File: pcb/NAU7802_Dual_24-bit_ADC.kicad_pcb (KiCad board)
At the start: 2 copper layers, 50.8 x 22.9 mm, 36 parts, among them J1 CELL_A, J2 CELL_B, J3 STEMMA_QT, J4 STEMMA_QT, M1 Feather_M4_Express, U1 NAU7802

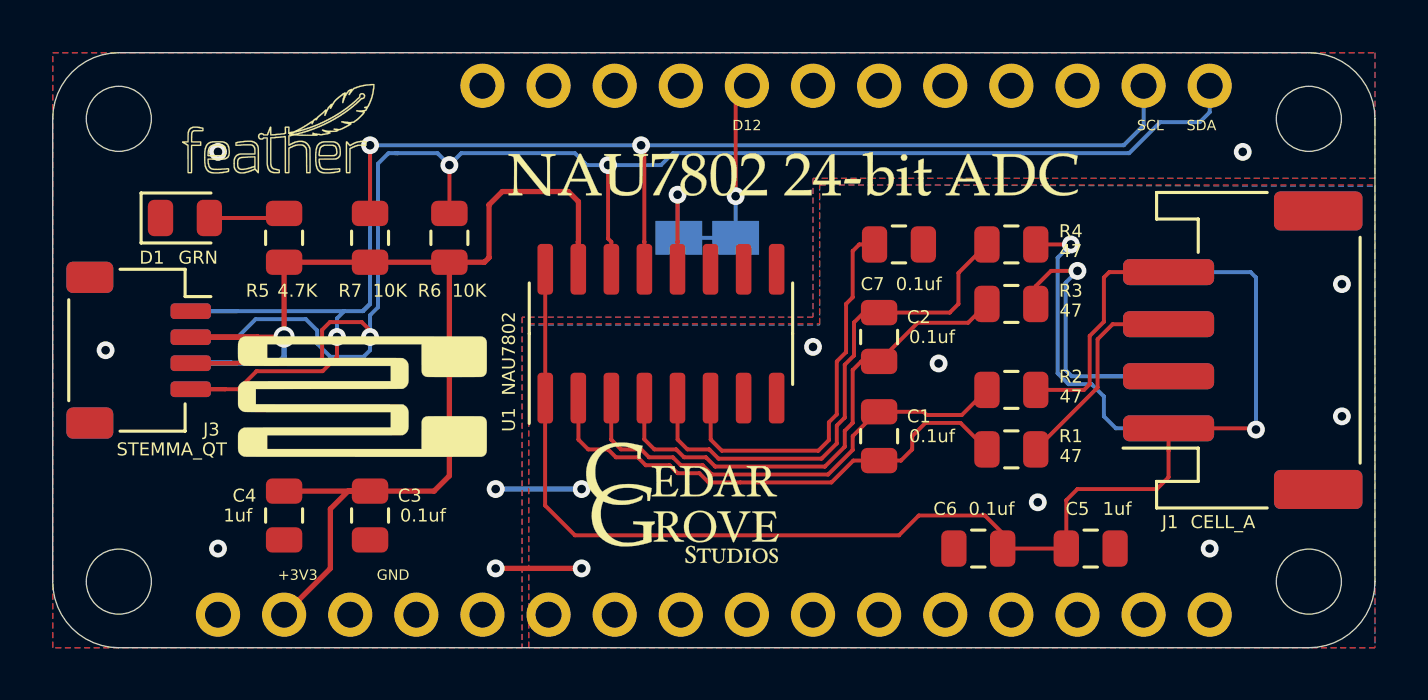
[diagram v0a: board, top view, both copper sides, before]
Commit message: update for 2-channel operation
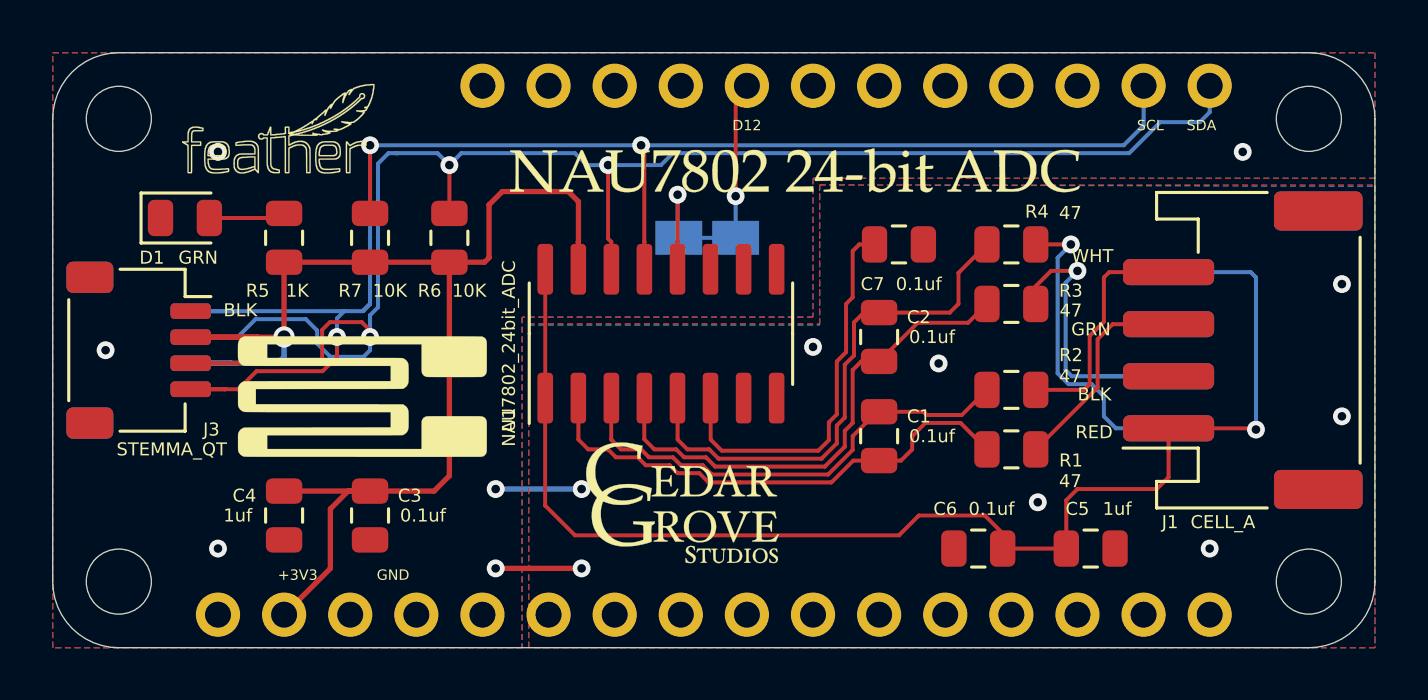
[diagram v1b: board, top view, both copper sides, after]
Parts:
- R5: value 4.7K -> 1K
- U1: value NAU7802 -> NAU7802_24bit_ADC
- moved G*** 0.15 mm to (156.8, 94.7)
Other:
- board text added: "2020-11-26 v01"
- board text added: "BLK"
- board text added: "GRN"
- board text added: "RED"
- board text added: "WHT"
- board text removed: "2020-10-21 v00"

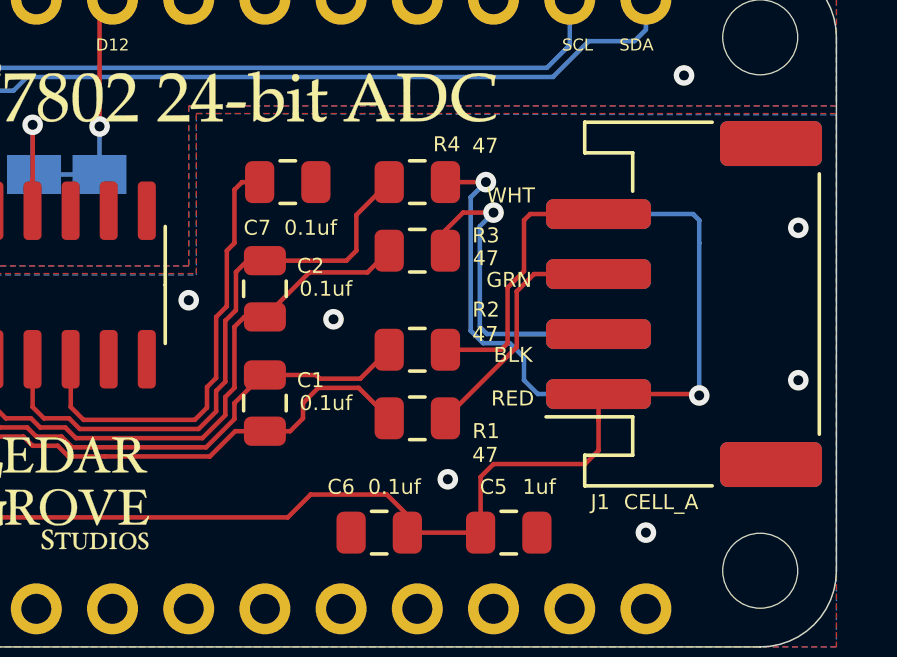
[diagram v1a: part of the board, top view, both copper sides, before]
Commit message: update PCB silk design
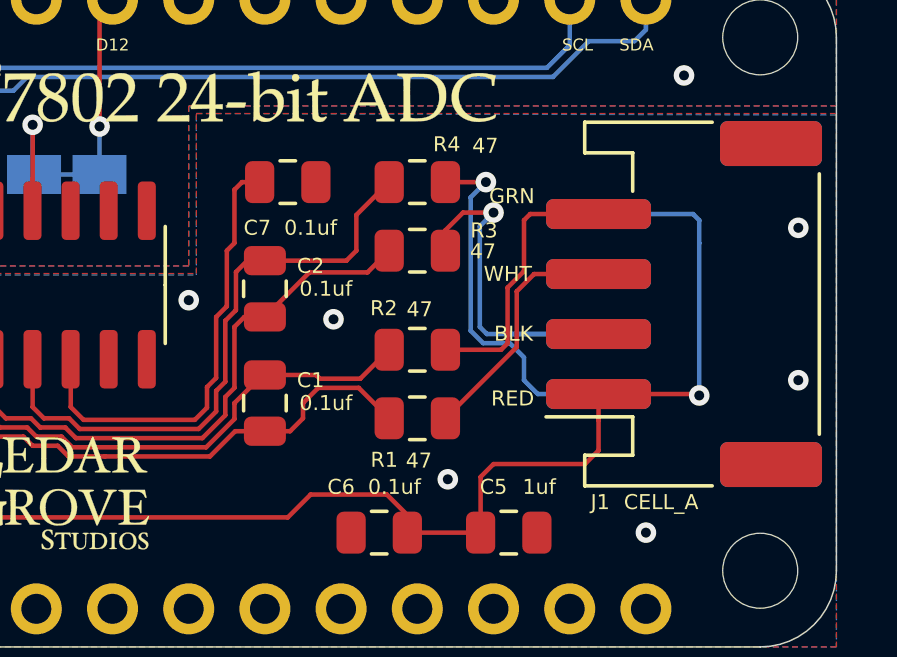
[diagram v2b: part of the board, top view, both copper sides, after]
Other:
- board text added: "2020-11-27 v01"
- board text removed: "2020-11-26 v01"

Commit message: update PCB design
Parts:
- moved R1 2.29 mm to (165.1, 103.1)
- moved R2 2.29 mm to (165.1, 105.4)
- moved C2 1.05 mm to (161.0, 100.8)
- moved C1 1.02 mm to (161.0, 104.8), turned to 270 degrees
- moved G*** 0.90 mm to (153.4, 107.3)
- renumbered e to REF
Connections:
- J1 pad 1: /AVDD -> /CELL_A+
- J1 pad 2: GND -> /CELL_A-
- J1 pad 3: /CELL_A- -> /AVDD
- J1 pad 4: /CELL_A+ -> GND
- J2 pad 1: /AVDD -> /CELL_B+
- J2 pad 2: GND -> /CELL_B-
- J2 pad 3: /CELL_B- -> /AVDD
- J2 pad 4: /CELL_B+ -> GND
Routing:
- net /CELL_B+: track 12.1 -> 5.54 mm
- net /CELL_B-: track 13.6 -> 7.77 mm
- net /CELL_A+: track 9.06 -> 5.19 mm
- net Net-(C7-Pad1): track 15.1 -> 11.5 mm
- net /CELL_A-: track 8.18 -> 5.32 mm
- net /A+: track 18.3 -> 20.5 mm, vias 0 -> 2
- net /A-: track 19.7 -> 21.3 mm
- net GND: track 6.60 -> 7.58 mm, vias 14 -> 16
- net /AVDD: track 51.5 -> 52.4 mm
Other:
- board text added: "2020-11-28 v02"
- board text added: "D12/DRDY"
- board text removed: "2020-11-27 v01"
- board text removed: "D12"
